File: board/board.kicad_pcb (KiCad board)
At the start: 2 copper layers, 29 x 29 mm, 4 parts, among them J1 001_I2C, J2 011_GPIO, U1 ALED7709ATR

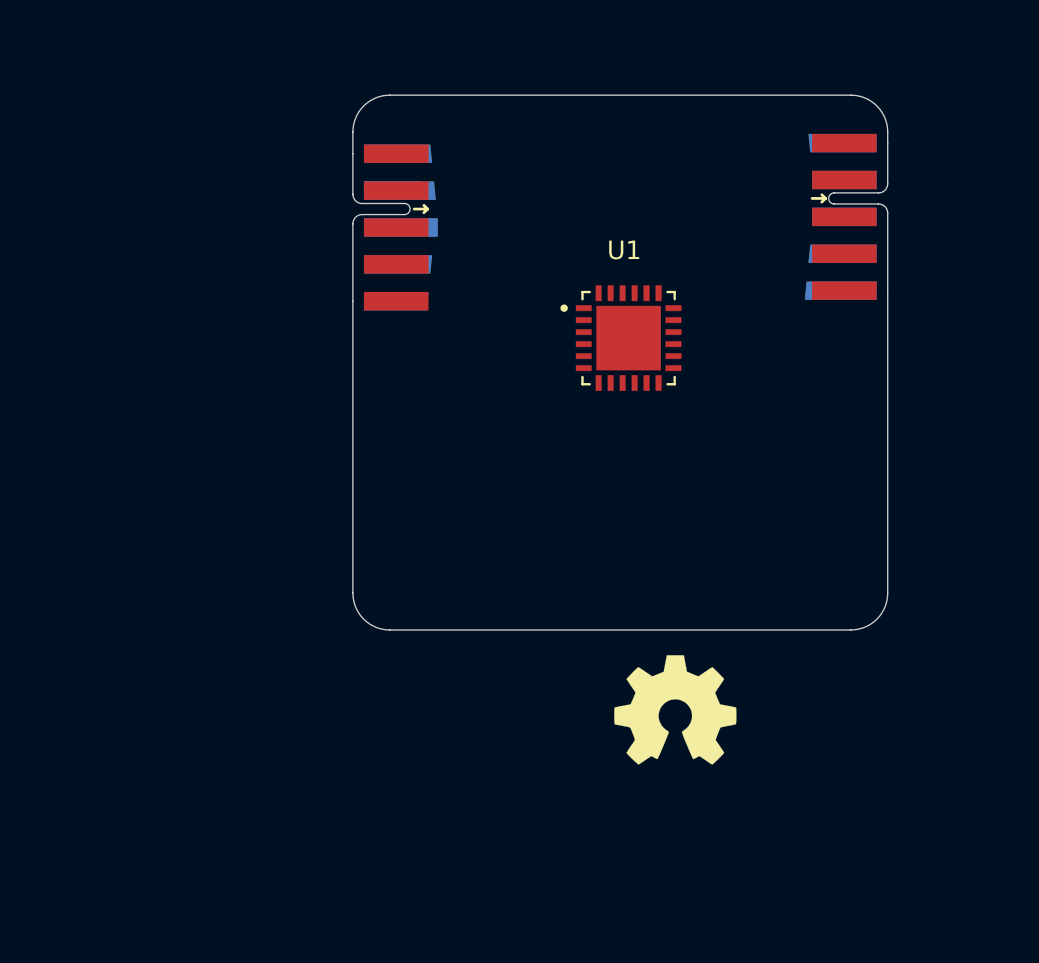
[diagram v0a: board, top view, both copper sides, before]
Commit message: Add footprint, symbol and 3D modell | Add parts for reference cicuit
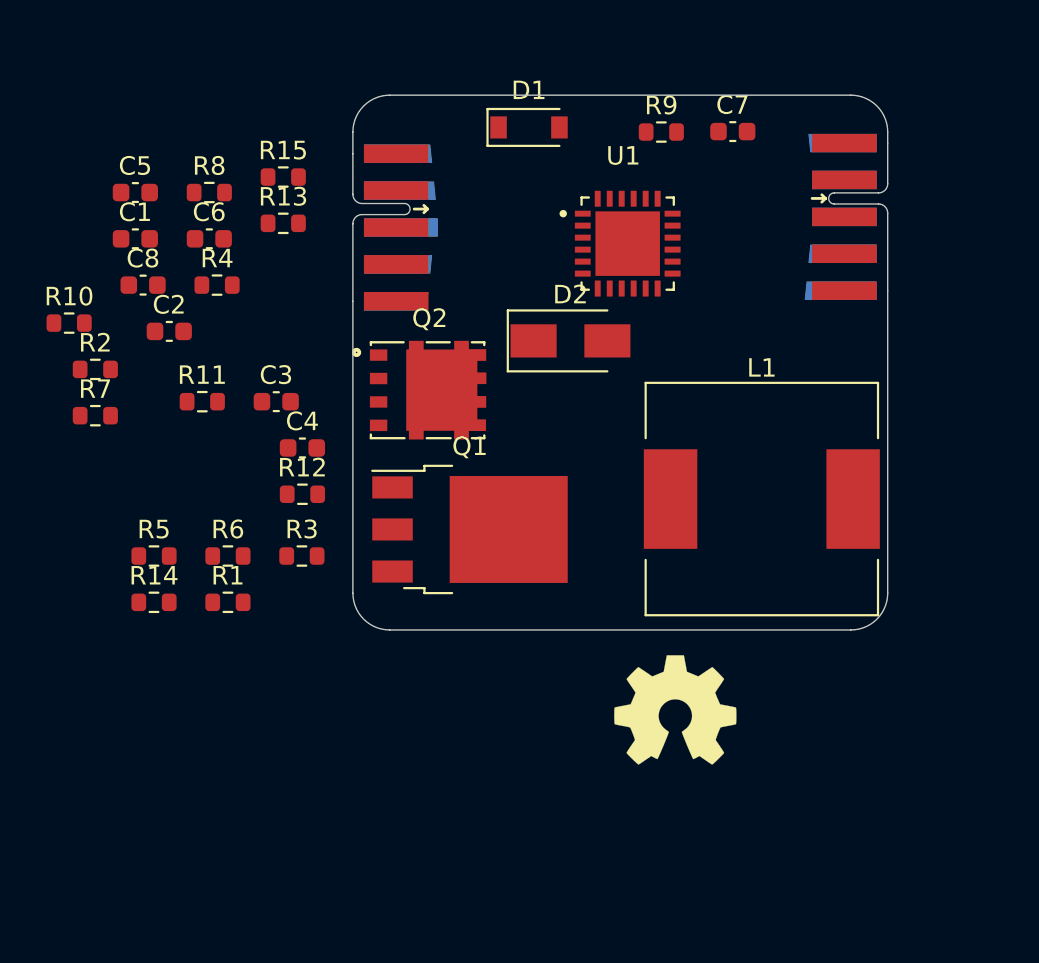
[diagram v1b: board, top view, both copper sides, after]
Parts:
- added C1: C_Small, Capacitor_SMD:C_0603_1608Metric, F.Cu at (128.2, 97.8)
- added C2: C_Small, Capacitor_SMD:C_0603_1608Metric, F.Cu at (130.0, 102.8)
- added C3: C_Small, Capacitor_SMD:C_0603_1608Metric, F.Cu at (135.8, 106.6)
- added C4: C_Small, Capacitor_SMD:C_0603_1608Metric, F.Cu at (137.3, 109.1)
- added C5: C_Small, Capacitor_SMD:C_0603_1608Metric, F.Cu at (128.2, 95.3)
- added C6: C_Small, Capacitor_SMD:C_0603_1608Metric, F.Cu at (132.2, 97.8)
- added C7: C_Small, Capacitor_SMD:C_0603_1608Metric, F.Cu at (160.6, 92.0)
- added C8: C_Small, Capacitor_SMD:C_0603_1608Metric, F.Cu at (128.6, 100.3)
- added D1: D_Schottky, Diode_SMD:D_SOD-123, F.Cu at (149.6, 91.8)
- added D2: D_Schottky, Diode_SMD:D_SMA, F.Cu at (151.8, 103.3)
- added L1: L, Inductor_SMD:L_12x12mm_H6mm, F.Cu at (162.2, 111.9)
- added Q1: Q_PMOS_DGS, Package_TO_SOT_SMD:TO-252-3_TabPin2, F.Cu at (146.3, 113.5)
- added Q2: Q_NMOS_DGS, led_treiber_edgy:TRANS_STL60P4LLF6, F.Cu at (144.1, 106.0)
- added R1: R_Small, Resistor_SMD:R_0603_1608Metric, F.Cu at (133.2, 117.5)
- added R10: R_Small, Resistor_SMD:R_0603_1608Metric, F.Cu at (124.6, 102.4)
- added R11: R_Small, Resistor_SMD:R_0603_1608Metric, F.Cu at (131.8, 106.6)
- added R12: R_Small, Resistor_SMD:R_0603_1608Metric, F.Cu at (137.3, 111.6)
- added R13: R_Small, Resistor_SMD:R_0603_1608Metric, F.Cu at (136.2, 97.0)
- added R14: R_Small, Resistor_SMD:R_0603_1608Metric, F.Cu at (129.2, 117.5)
- added R15: R_Small, Resistor_SMD:R_0603_1608Metric, F.Cu at (136.2, 94.4)
- added R2: R_Small, Resistor_SMD:R_0603_1608Metric, F.Cu at (126.0, 104.9)
- added R3: R_Small, Resistor_SMD:R_0603_1608Metric, F.Cu at (137.2, 115.0)
- added R4: R_Small, Resistor_SMD:R_0603_1608Metric, F.Cu at (132.6, 100.3)
- added R5: R_Small, Resistor_SMD:R_0603_1608Metric, F.Cu at (129.2, 115.0)
- added R6: R_Small, Resistor_SMD:R_0603_1608Metric, F.Cu at (133.2, 115.0)
- added R7: R_Small, Resistor_SMD:R_0603_1608Metric, F.Cu at (126.0, 107.4)
- added R8: R_Small, Resistor_SMD:R_0603_1608Metric, F.Cu at (132.2, 95.3)
- added R9: R_Small, Resistor_SMD:R_0603_1608Metric, F.Cu at (156.7, 92.0)
- moved U1 5.13 mm to (154.9, 98.0)
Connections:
- J1 pad 1: unconnected-(J1-Pad1) -> GND
- J1 pad 10: unconnected-(J1-Pad10) -> /implementation/VIN
- J1 pad 2: unconnected-(J1-Pad2) -> /implementation/SDA
- J1 pad 3: unconnected-(J1-Pad3) -> /implementation/SCL
- J1 pad 4: unconnected-(J1-Pad4) -> /implementation/Enable
- J1 pad 6: (no net) -> /implementation/PWMI
- J1 pad 7: (no net) -> /implementation/Fault
- J2 pad 1: unconnected-(J2-Pad1) -> GND
- J2 pad 10: unconnected-(J2-Pad10) -> /implementation/common_Anode
- J2 pad 2: unconnected-(J2-Pad2) -> /implementation/CH1
- J2 pad 3: unconnected-(J2-Pad3) -> /implementation/CH2
- J2 pad 4: unconnected-(J2-Pad4) -> /implementation/CH3
- J2 pad 5: unconnected-(J2-Pad5) -> /implementation/CH4
- J2 pad 8: unconnected-(J2-Pad8) -> GND
- U1 pad 1: unconnected-(U1-Pad1) -> /implementation/Enable
- U1 pad 10: CH3 -> /implementation/CH3
- U1 pad 11: CH4 -> /implementation/CH4
- U1 pad 12: unconnected-(U1-Pad12) -> GND
- U1 pad 13: unconnected-(U1-Pad13) -> Net-(U1-Pad13)
- U1 pad 14: unconnected-(U1-Pad14) -> Net-(U1-Pad14)
- U1 pad 15: unconnected-(U1-Pad15) -> Net-(U1-Pad15)
- U1 pad 16: unconnected-(U1-Pad16) -> Net-(U1-Pad16)
- U1 pad 17: unconnected-(U1-Pad17) -> Net-(U1-Pad17)
- U1 pad 18: unconnected-(U1-Pad18) -> Net-(U1-Pad18)
- U1 pad 19: unconnected-(U1-Pad19) -> Net-(U1-Pad19)
- U1 pad 2: unconnected-(U1-Pad2) -> Net-(U1-Pad2)
- U1 pad 20: unconnected-(U1-Pad20) -> Net-(U1-Pad20)
- U1 pad 21: unconnected-(U1-Pad21) -> Net-(U1-Pad21)
- U1 pad 22: unconnected-(U1-Pad22) -> Net-(U1-Pad22)
- U1 pad 23: unconnected-(U1-Pad23) -> Net-(U1-Pad23)
- U1 pad 24: unconnected-(U1-Pad24) -> /implementation/VIN
- U1 pad 3: unconnected-(U1-Pad3) -> Net-(U1-Pad3)
- U1 pad 4: unconnected-(U1-Pad4) -> /implementation/SDA
- U1 pad 5: unconnected-(U1-Pad5) -> /implementation/SCL
- U1 pad 6: unconnected-(U1-Pad6) -> /implementation/Fault
- U1 pad 7: unconnected-(U1-Pad7) -> /implementation/PWMI
- U1 pad 8: CH1 -> /implementation/CH1
- U1 pad 9: CH2 -> /implementation/CH2

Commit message: Add routing
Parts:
- C1, C2, C3, C4, C5, C6, C7, C8: footprint Capacitor_SMD:C_0603_1608Metric -> Capacitor_SMD:C_0402_1005Metric
- L1: footprint Inductor_SMD:L_12x12mm_H6mm -> led_treiber_edgy:IND_XGL1010-332MED
- LOGO1: moved to B.Cu
- R1, R10, R11, R12, R13, R14, R15, R2, R3, R4, R5, R6, R7, R8, R9: footprint Resistor_SMD:R_0603_1608Metric -> Resistor_SMD:R_0402_1005Metric
- moved R5 35.9 mm to (157.3, 92.7), turned to -90 degrees
- moved R10 35.0 mm to (158.3, 92.7), turned to 90 degrees
- moved R1 34.1 mm to (162.5, 100.1), turned to 180 degrees
- moved R14 34.0 mm to (152.4, 92.7), turned to -90 degrees
- moved R6 32.1 mm to (156.3, 92.7), turned to -90 degrees
- moved R12 30.6 mm to (160.0, 91.2), turned to 180 degrees
- moved R2 28.4 mm to (154.4, 102.5), turned to 90 degrees
- moved R4 28.3 mm to (160.0, 93.2), turned to 180 degrees
- moved C2 27.5 mm to (154.8, 91.0)
- moved R7 27.0 mm to (151.9, 99.7), turned to 180 degrees
- moved R11 25.7 mm to (153.4, 92.7), turned to -90 degrees
- moved C6 25.5 mm to (157.3, 102.5), turned to -90 degrees
- moved C5 24.8 mm to (150.6, 105.9)
- moved R15 24.3 mm to (159.2, 102.4), turned to 90 degrees
- moved R13 24.2 mm to (160.0, 92.2)
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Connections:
- J2 pad 2: /implementation/CH1 -> /implementation/CH4
- J2 pad 3: /implementation/CH2 -> /implementation/CH3
- J2 pad 4: /implementation/CH3 -> /implementation/CH2
- J2 pad 5: /implementation/CH4 -> /implementation/CH1
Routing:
- net GND: track 0.00 -> 50.4 mm, vias 0 -> 1
- net /implementation/common_Anode: track 0.00 -> 37.8 mm, vias 0 -> 2
- net Net-(D1-K): track 0.00 -> 35.4 mm, vias 0 -> 2
- net /implementation/PWMI: track 0.00 -> 34.5 mm, vias 0 -> 2
- net Net-(Q1-G): track 0.00 -> 29.2 mm, vias 0 -> 2
- net Net-(Q1-D): track 0.00 -> 25.7 mm
- net /implementation/SCL: track 0.00 -> 23.5 mm, vias 0 -> 2
- net /implementation/Fault: track 0.00 -> 22.9 mm, vias 0 -> 2
- net /implementation/SDA: track 0.00 -> 21.6 mm, vias 0 -> 2
- net Net-(Q2-S): track 0.00 -> 21.3 mm, vias 0 -> 3
- net /implementation/VIN: track 0.00 -> 18.0 mm, vias 0 -> 2
- net /implementation/Enable: track 0.00 -> 17.0 mm, vias 0 -> 2
- net Net-(Q2-G): track 0.00 -> 15.6 mm, vias 0 -> 2
- net Net-(U1-LDO3V3): track 0.00 -> 14.9 mm, vias 0 -> 2
- net Net-(D2-A): track 0.00 -> 13.3 mm, vias 0 -> 2
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- added copper zone on F.Cu, net GND
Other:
- copper layers 2 -> 4

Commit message: Update PCB
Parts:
- added CS1: TestPoint, TestPoint:TestPoint_Pad_D1.0mm, F.Cu at (161.2, 91.3)
- added D_Q2: TestPoint, TestPoint:TestPoint_Pad_D1.0mm, F.Cu at (165.5, 104.6)
- added D_Q3: TestPoint, TestPoint:TestPoint_Pad_D1.0mm, F.Cu at (154.8, 104.3)
- added G_Q2: TestPoint, TestPoint:TestPoint_Pad_D1.0mm, F.Cu at (165.5, 106.7)
- added G_Q3: TestPoint, TestPoint:TestPoint_Pad_D1.0mm, F.Cu at (152.7, 104.0)
- added PWMI1: TestPoint, TestPoint:TestPoint_Pad_D1.0mm, F.Cu at (146.8, 91.8)
- added SCL1: TestPoint, TestPoint:TestPoint_Pad_D1.0mm, F.Cu at (155.9, 91.2)
- added SDA1: TestPoint, TestPoint:TestPoint_Pad_D1.0mm, F.Cu at (158.6, 91.2)
- added S_Q2: TestPoint, TestPoint:TestPoint_Pad_D1.0mm, F.Cu at (165.5, 108.7)
- added S_Q3: TestPoint, TestPoint:TestPoint_Pad_D1.0mm, F.Cu at (140.9, 103.9)
- added TH1: 10kΩ, Resistor_SMD:R_0603_1608Metric, F.Cu at (158.2, 95.1)
- C1, C8: value C_Small -> 10uF
- C4, C6, C7: value C_Small -> 1uF
- L1: value L -> 15uH
- R10: value R_Small -> 2kΩ
- R12: value R_Small -> 1,8kΩ
- R13: value R_Small -> 1.1kΩ
- R4: value R_Small -> 6,8kΩ
- R5: value R_Small -> 62kΩ
- R7: value R_Small -> 39 mΩ
- moved D1 20.7 mm to (144.3, 103.9), turned to 0 degrees
- moved L1 16.2 mm to (147.2, 111.0), turned to 0 degrees
- moved R8 15.0 mm to (154.2, 113.0), turned to 0 degrees
- moved Q1 14.6 mm to (160.8, 115.3), turned to 0 degrees
- moved R4 13.9 mm to (146.3, 95.9), turned to 90 degrees
- moved C8 13.7 mm to (161.9, 101.4), turned to 90 degrees
- moved C2 13.7 mm to (146.3, 101.7), turned to -90 degrees
- moved Q2 12.9 mm to (158.0, 108.8), turned to 0 degrees
- moved R14 11.7 mm to (148.2, 103.6)
- moved R11 11.7 mm to (149.2, 103.6)
- moved R5 11.5 mm to (146.8, 97.3), turned to 0 degrees
- moved R6 11.1 mm to (146.8, 98.3), turned to 0 degrees
- moved R1 11.0 mm to (153.6, 93.5), turned to -90 degrees
- moved C3 10.8 mm to (146.8, 99.3), turned to 180 degrees
- moved R9 10.7 mm to (146.8, 100.3), turned to 0 degrees
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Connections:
- J1 pad 9: unconnected-(J1-3.3V-Pad9) -> 3.3V
- J2 pad 9: unconnected-(J2-3.3V-Pad9) -> 3.3V
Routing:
- net GND: track 50.4 -> 23.8 mm, vias 1 -> 7
- net 3.3V: track 0.00 -> 25.3 mm
- net /implementation/PWMI: track 34.5 -> 15.2 mm, vias 2 -> 1
- net /implementation/Enable: track 17.0 -> 33.3 mm, vias 2 -> 3
- net Net-(U1-TSNS): track 1.88 -> 18.0 mm, vias 0 -> 2
- net /implementation/common_Anode: track 37.8 -> 25.1 mm
- net /implementation/CH4: track 7.68 -> 19.9 mm, vias 0 -> 2
- net /implementation/CH3: track 7.12 -> 19.0 mm, vias 0 -> 2
- net Net-(D2-A): track 13.3 -> 24.8 mm
- net /implementation/CH2: track 7.22 -> 18.6 mm, vias 0 -> 2
- net Net-(U1-LDO3V3): track 14.9 -> 3.84 mm, vias 2 -> 0
- net /implementation/VIN: track 18.0 -> 27.8 mm
- net /implementation/CH1: track 7.78 -> 17.6 mm, vias 0 -> 2
- net Net-(D1-K): track 35.4 -> 26.6 mm, vias 2 -> 0
- net Net-(Q1-D): track 25.7 -> 18.2 mm, vias 0 -> 2
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- added copper zone on B.Cu, net GND
- added copper zone on In1.Cu, net GND
- added copper zone on In2.Cu, net GND

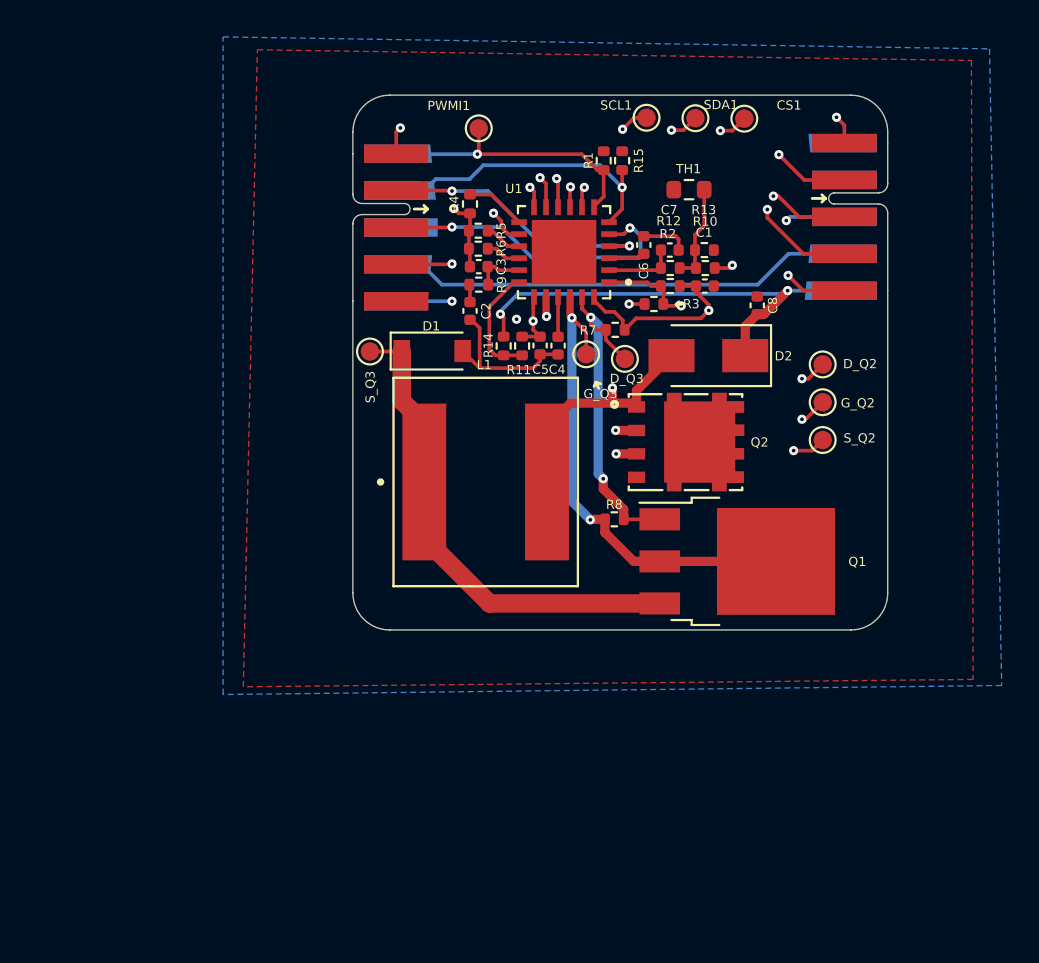
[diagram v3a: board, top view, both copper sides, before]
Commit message: Update footprint for MOSFETS
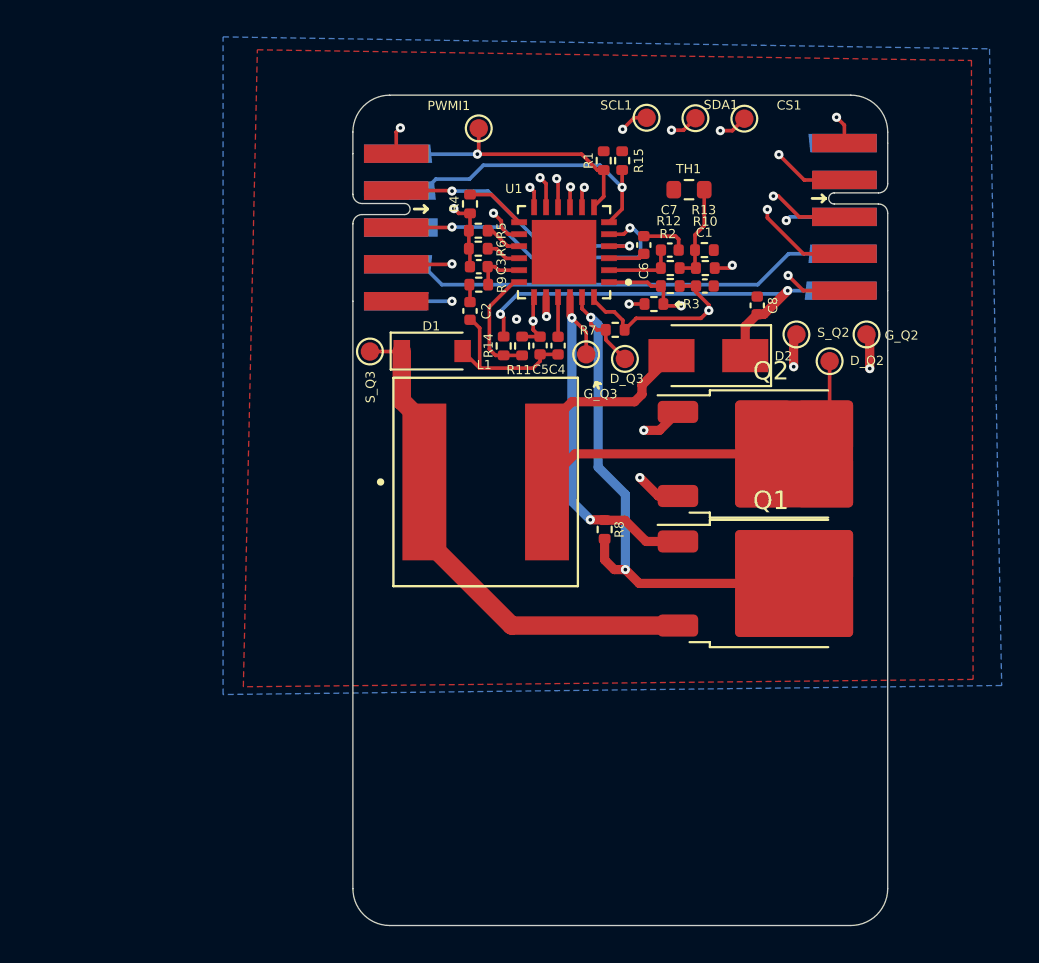
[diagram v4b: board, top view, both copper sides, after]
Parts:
- D1, D2: value D_Schottky -> ~
- Q1: value Q_PMOS_DGS -> ~; footprint Package_TO_SOT_SMD:TO-252-3_TabPin2 -> Package_TO_SOT_SMD:TO-252-2
- Q2: value Q_NMOS_DGS -> ~; footprint led_treiber_edgy:TRANS_STL60P4LLF6 -> Package_TO_SOT_SMD:TO-252-2
- moved S_Q2 5.90 mm to (164.1, 103.0)
- moved Q2 4.67 mm to (162.7, 109.5)
- moved G_Q2 4.38 mm to (167.8, 103.0)
- moved Q1 2.18 mm to (162.7, 116.5)
- moved R8 0.76 mm to (153.7, 113.5), turned to -90 degrees
- moved D_Q2 0.41 mm to (165.8, 104.4)
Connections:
- Q1 pad 1: Net-(Q1-D) -> Net-(Q1-G)
- Q1 pad 2: Net-(Q1-G) -> Net-(Q1-D)
- Q2 pad 1: Net-(D2-A) -> Net-(Q2-G)
- Q2 pad 2: Net-(Q2-G) -> Net-(D2-A)
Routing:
- net Net-(Q1-D): track 18.2 -> 31.0 mm
- net Net-(Q2-G): track 21.8 -> 28.8 mm
- net Net-(Q1-G): track 26.3 -> 20.1 mm
- net Net-(Q2-S): track 25.0 -> 30.1 mm
- net Net-(D2-A): track 24.8 -> 29.3 mm, vias 2 -> 0
- net Net-(D1-K): track 26.6 -> 28.1 mm
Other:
- board size 29 x 29 mm -> 29 x 45 mm
